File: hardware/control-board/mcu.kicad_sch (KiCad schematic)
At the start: 35 parts, among them J2 USB_C_Receptacle, SW29 USB Boot, SW30 Reset, U5 RP2040, U6 W25Q16JVUU, U7 XC6206P332MR, U8 USBLC6-2SC6, Y1 12MHz

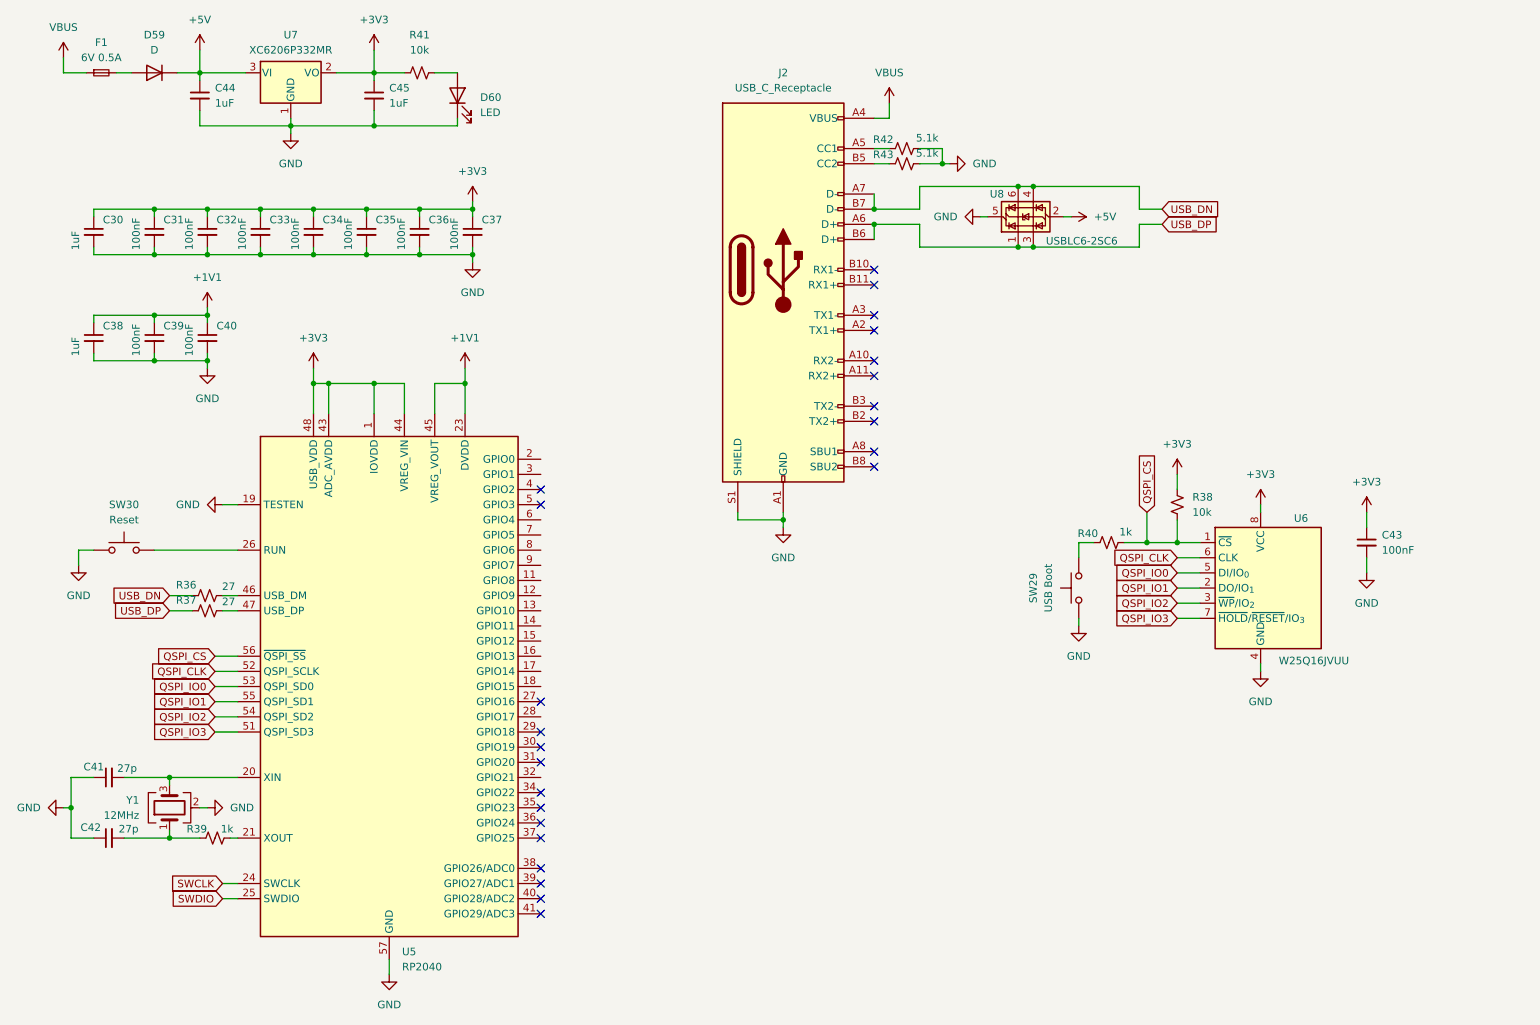
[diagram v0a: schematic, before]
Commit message: mcu controller added
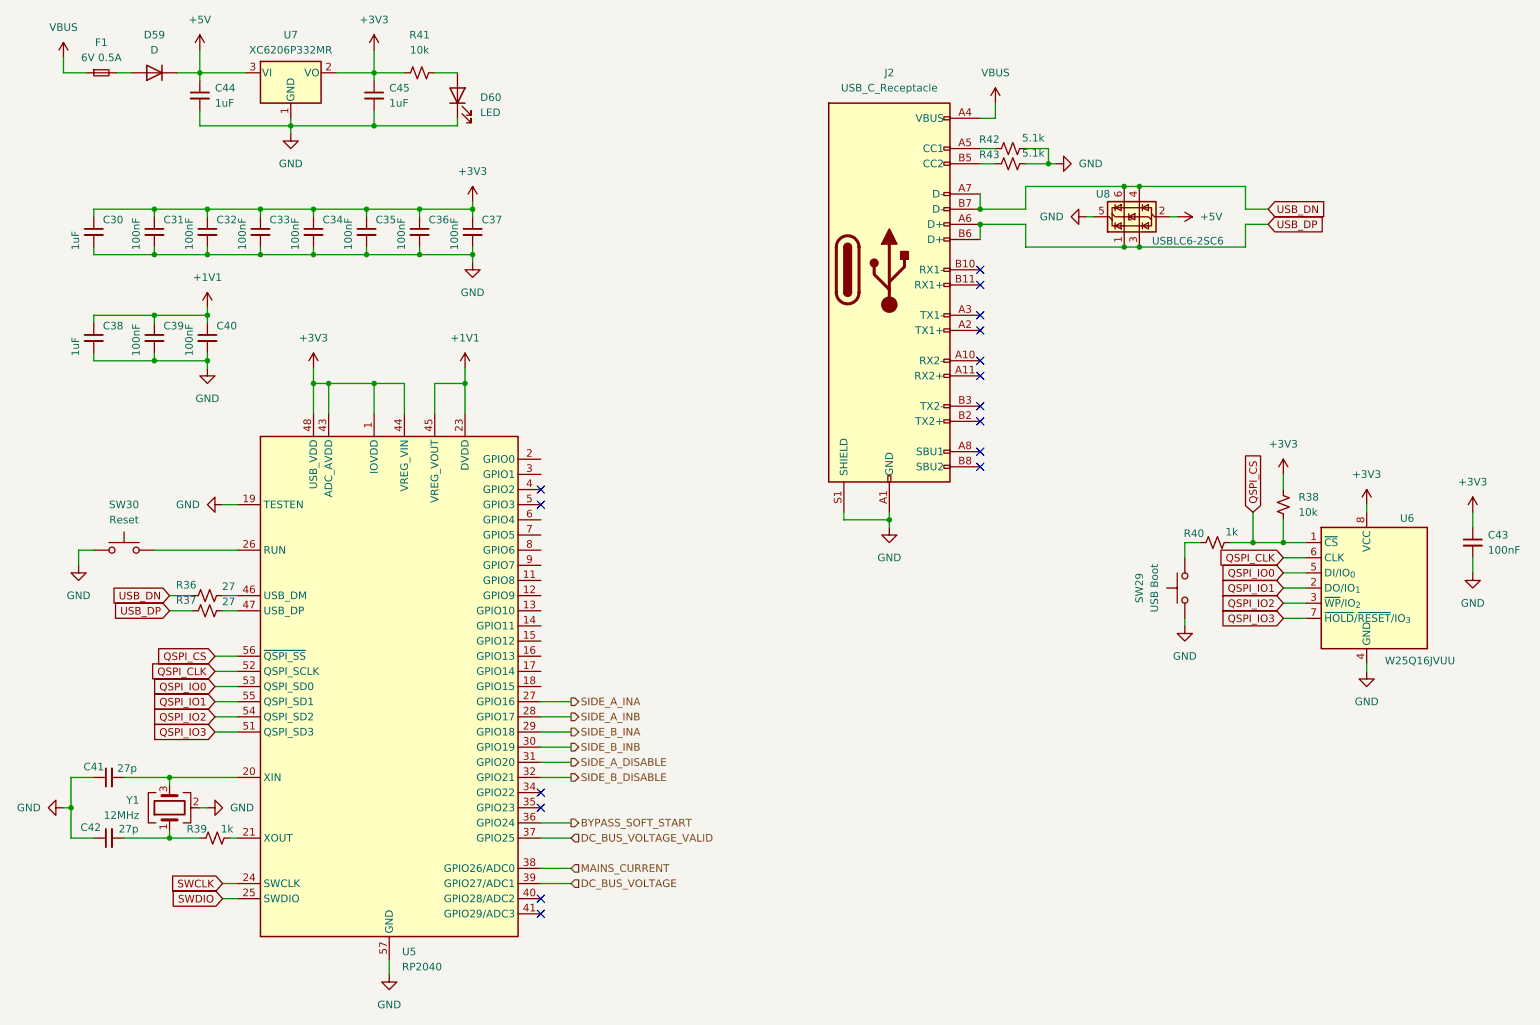
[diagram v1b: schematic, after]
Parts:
- J2: footprint (none) -> Connector_USB:USB_C_Receptacle_GCT_USB4105-xx-A_16P_TopMnt_Horizontal
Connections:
- net SIDE_A_INA: now reaches U5.27 (GPIO16)
- net SIDE_A_INB: now reaches U5.28 (GPIO17)
- net SIDE_B_INA: now reaches U5.29 (GPIO18)
- net SIDE_B_INB: now reaches U5.30 (GPIO19)
- net SIDE_A_DISABLE: now reaches U5.31 (GPIO20)
- net SIDE_B_DISABLE: now reaches U5.32 (GPIO21)
- net BYPASS_SOFT_START: now reaches U5.36 (GPIO24)
- net DC_BUS_VOLTAGE_VALID: now reaches U5.37 (GPIO25)
- net MAINS_CURRENT: now reaches U5.38 (GPIO26/ADC0)
- net DC_BUS_VOLTAGE: now reaches U5.39 (GPIO27/ADC1)
- no-connect marks 24 -> 16
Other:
- moved on the sheet: C43, J2, R38, R40, R42, R43, SW29, U6, U8
